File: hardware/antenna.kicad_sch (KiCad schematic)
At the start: 8 parts

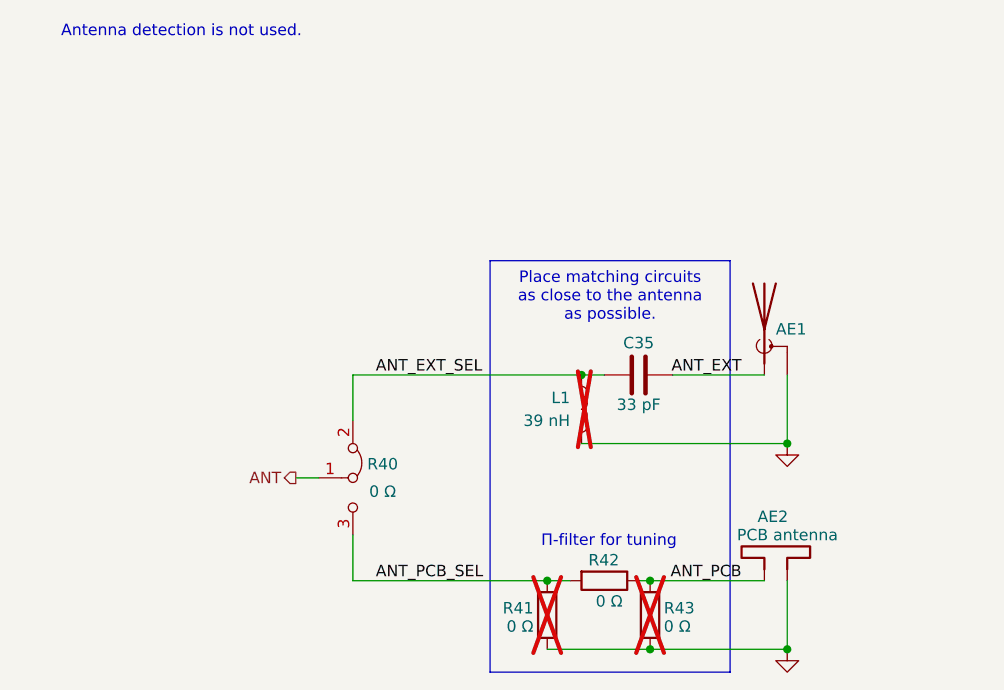
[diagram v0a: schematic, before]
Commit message: HW: Update components to be hand solderable
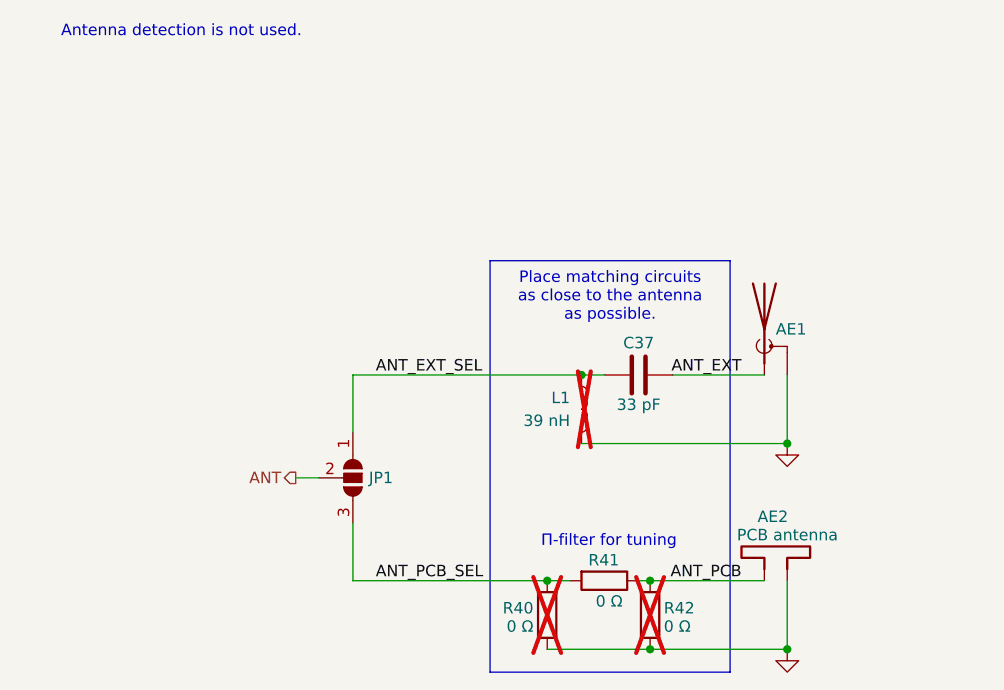
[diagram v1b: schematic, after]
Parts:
- removed R40: 0 Ω, perfect_footprints:0hm_choice, symbol perfect_footprints:0hm_choice
- added JP1: SolderJumper_3_Open, Jumper:SolderJumper-3_P2.0mm_Open_TrianglePad1.0x1.5mm, symbol Jumper:SolderJumper_3_Open
- C37: renamed from C35; footprint perfect_footprints:0402_1005_perfect -> Capacitor_SMD:C_0402_1005Metric_Pad0.74x0.62mm_HandSolder
- L1: footprint Inductor_SMD:L_0603_1608Metric -> Inductor_SMD:L_0603_1608Metric_Pad1.05x0.95mm_HandSolder
- R40: renamed from R41; footprint perfect_footprints:0402_1005_perfect -> Resistor_SMD:R_0402_1005Metric_Pad0.72x0.64mm_HandSolder
- R41: renamed from R42; footprint perfect_footprints:0402_1005_perfect -> Resistor_SMD:R_0402_1005Metric_Pad0.72x0.64mm_HandSolder
- R42: renamed from R43; footprint perfect_footprints:0402_1005_perfect -> Resistor_SMD:R_0402_1005Metric_Pad0.72x0.64mm_HandSolder
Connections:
- net ANT: now also JP1.2 (C)
- net ANT_EXT_SEL: now also JP1.1 (A)
- net ANT_PCB_SEL: now also JP1.3 (B)
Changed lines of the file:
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@@
 	(wire
 		(pts
-			(xy 101.6 106.68) (xy 101.6 111.76)
+			(xy 101.6 105.41) (xy 101.6 111.76)
 		)
 		(stroke
@@
 	(wire
 		(pts
-			(xy 101.6 88.9) (xy 101.6 93.98)
+			(xy 147.32 111.76) (xy 134.62 111.76)
 		)
 		(stroke
@@
 	(wire
 		(pts
-			(xy 147.32 111.76) (xy 134.62 111.76)
+			(xy 125.73 111.76) (xy 123.19 111.76)
 		)
 		(stroke
@@
 	(wire
 		(pts
-			(xy 125.73 111.76) (xy 123.19 111.76)
+			(xy 101.6 88.9) (xy 127 88.9)
 		)
 		(stroke
@@
 	(wire
 		(pts
-			(xy 101.6 88.9) (xy 127 88.9)
+			(xy 147.32 88.9) (xy 137.16 88.9)
 		)
 		(stroke
@@
 	(wire
 		(pts
-			(xy 147.32 88.9) (xy 137.16 88.9)
+			(xy 149.86 119.38) (xy 134.62 119.38)
 		)
 		(stroke
@@
 	(wire
 		(pts
-			(xy 149.86 119.38) (xy 134.62 119.38)
+			(xy 134.62 111.76) (xy 133.35 111.76)
 		)
 		(stroke
@@
 	(wire
 		(pts
-			(xy 134.62 111.76) (xy 133.35 111.76)
+			(xy 101.6 88.9) (xy 101.6 95.25)
 		)
 		(stroke
@@
 		(on_board yes)
 		(dnp no)
-		(property "Reference" "C35"
+		(property "Reference" "C37"
 			(at 133.35 85.344 90)
 			(effects
@@
 			)
 		)
-		(property "Footprint" "perfect_footprints:0402_1005_perfect"
+		(property "Footprint" "Capacitor_SMD:C_0402_1005Metric_Pad0.74x0.62mm_HandSolder"
 			(at 129.54 87.9348 0)
 			(effects
@@
 			(project "iida_devkit"
 				(path "/b12a6e25-97fb-4aba-bc96-af8db389bb9a/6e456e95-dbda-43fc-b148-815c3be21ba0"
-					(reference "C35")
+					(reference "C37")
 					(unit 1)
 				)
@@
 		(on_board yes)
 		(dnp no)
-		(property "Reference" "R42"
+		(property "Reference" "R41"
 			(at 127.762 109.474 90)
 			(effects
@@
 			)
 		)
-		(property "Footprint" "perfect_footprints:0402_1005_perfect"
+		(property "Footprint" "Resistor_SMD:R_0402_1005Metric_Pad0.72x0.64mm_HandSolder"
 			(at 129.54 109.982 90)
 			(effects
@@
 			(project "iida_devkit"
 				(path "/b12a6e25-97fb-4aba-bc96-af8db389bb9a/6e456e95-dbda-43fc-b148-815c3be21ba0"
-					(reference "R42")
+					(reference "R41")
 					(unit 1)
 				)
@@
 			)
 		)
-		(property "Footprint" "Inductor_SMD:L_0603_1608Metric"
+		(property "Footprint" "Inductor_SMD:L_0603_1608Metric_Pad1.05x0.95mm_HandSolder"
 			(at 127 92.71 0)
 			(effects
@@
 		(dnp no)
 		(fields_autoplaced yes)
-		(property "Reference" "#PWR054"
+		(property "Reference" "#PWR060"
 			(at 149.86 125.73 0)
 			(effects
@@
 			(project "iida_devkit"
 				(path "/b12a6e25-97fb-4aba-bc96-af8db389bb9a/6e456e95-dbda-43fc-b148-815c3be21ba0"
-					(reference "#PWR054")
+					(reference "#PWR060")
 					(unit 1)
 				)
@@
 		(on_board yes)
 		(dnp yes)
-		(property "Reference" "R41"
+		(property "Reference" "R40"
 			(at 121.666 114.808 0)
 			(effects
@@
 			)
 		)
-		(property "Footprint" "perfect_footprints:0402_1005_perfect"
+		(property "Footprint" "Resistor_SMD:R_0402_1005Metric_Pad0.72x0.64mm_HandSolder"
 			(at 121.412 115.57 90)
 			(effects
@@
 			(project "iida_devkit"
 				(path "/b12a6e25-97fb-4aba-bc96-af8db389bb9a/6e456e95-dbda-43fc-b148-815c3be21ba0"
-					(reference "R41")
+					(reference "R40")
 					(unit 1)
 				)
@@
 		(on_board yes)
 		(dnp yes)
-		(property "Reference" "R43"
+		(property "Reference" "R42"
 			(at 136.144 114.808 0)
 			(effects
@@
 			)
 		)
-		(property "Footprint" "perfect_footprints:0402_1005_perfect"
+		(property "Footprint" "Resistor_SMD:R_0402_1005Metric_Pad0.72x0.64mm_HandSolder"
 			(at 136.398 115.57 90)
 			(effects
@@
 			(project "iida_devkit"
 				(path "/b12a6e25-97fb-4aba-bc96-af8db389bb9a/6e456e95-dbda-43fc-b148-815c3be21ba0"
-					(reference "R43")
+					(reference "R42")
 					(unit 1)
 				)
@@
 	)
 	(symbol
-		(lib_id "perfect_footprints:0hm_choice")
+		(lib_id "Jumper:SolderJumper_3_Open")
 		(at 101.6 100.33 270)
 		(unit 1)
-		(exclude_from_sim no)
-		(in_bom yes)
+		(exclude_from_sim yes)
+		(in_bom no)
 		(on_board yes)
 		(dnp no)
-		(property "Reference" "R40"
-			(at 104.902 98.806 90)
+		(property "Reference" "JP1"
+			(at 103.378 100.33 90)
 			(effects
 				(font
 					(size 1.27 1.27)
 				)
+				(justify left)
 			)
 		)
-		(property "Value" "0 Ω"
-			(at 104.902 101.854 90)
+		(property "Value" "SolderJumper_3_Open"
+			(at 104.14 101.5999 90)
 			(effects
 				(font
 					(size 1.27 1.27)
 				)
+				(justify left)
+				(hide yes)
 			)
 		)
-		(property "Footprint" "perfect_footprints:0hm_choice"
-			(at 93.472 100.33 0)
+		(property "Footprint" "Jumper:SolderJumper-3_P2.0mm_Open_TrianglePad1.0x1.5mm"
+			(at 101.6 100.33 0)
 			(effects
 				(font
@@
 			)
 		)
-		(property "Datasheet" ""
-			(at 105.41 95.25 0)
+		(property "Datasheet" "~"
+			(at 101.6 100.33 0)
 			(effects
 				(font
@@
 			)
 		)
-		(property "Description" ""
-			(at 105.41 95.25 0)
+		(property "Description" "Solder Jumper, 3-pole, open"
+			(at 101.6 100.33 0)
 			(effects
 				(font
@@
 			)
 		)
-		(property "Digi-Key Part Number" "311-0.0JRCT-ND"
+		(property "Digi-Key Part Number" "-"
 			(at 101.6 100.33 0)
 			(effects
@@
 			)
 		)
-		(property "Manufacturer" "YAGEO"
+		(property "Manufacturer" "-"
 			(at 101.6 100.33 0)
 			(effects
@@
 			)
 		)
-		(property "Manufacturer Part Number" "RC0402JR-070RL"
+		(property "Manufacturer Part Number" "-"
 			(at 101.6 100.33 0)
 			(effects
@@
 		(pin "2"
 		)
-		(pin "3"
-		)
 		(pin "1"
 		)
+		(pin "3"
+		)
 		(instances
 			(project ""
 				(path "/b12a6e25-97fb-4aba-bc96-af8db389bb9a/6e456e95-dbda-43fc-b148-815c3be21ba0"
-					(reference "R40")
+					(reference "JP1")
 					(unit 1)
 				)
@@
 		(dnp no)
 		(fields_autoplaced yes)
-		(property "Reference" "#PWR053"
+		(property "Reference" "#PWR059"
 			(at 149.86 102.87 0)
 			(effects
@@
 			(project "iida_devkit"
 				(path "/b12a6e25-97fb-4aba-bc96-af8db389bb9a/6e456e95-dbda-43fc-b148-815c3be21ba0"
-					(reference "#PWR053")
+					(reference "#PWR059")
 					(unit 1)
 				)

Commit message: HW: Update components, change footprints to handsolder versions, finish power
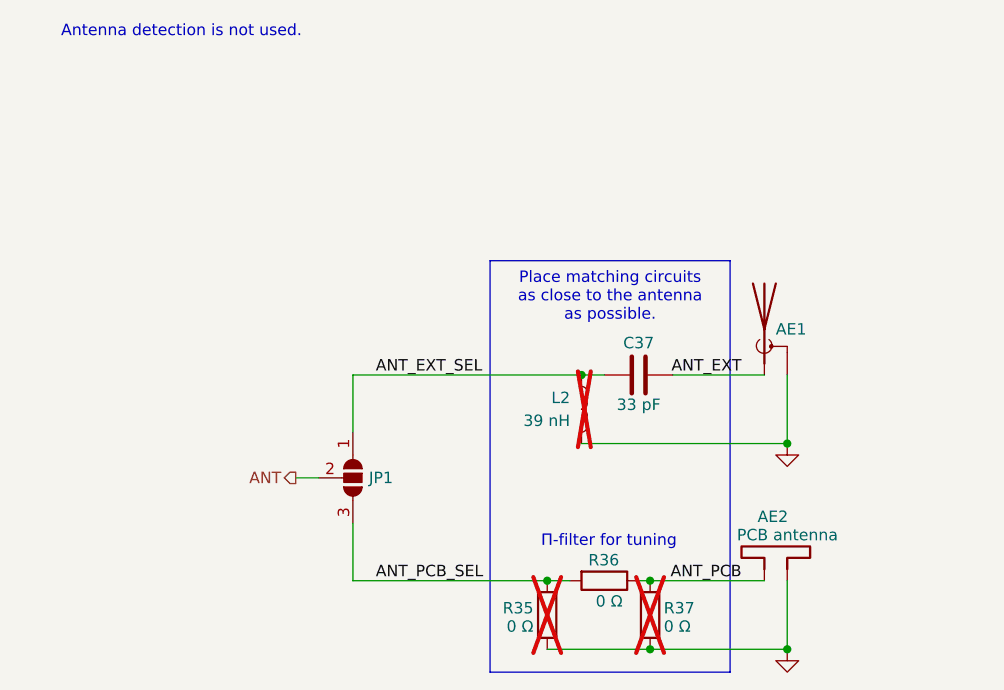
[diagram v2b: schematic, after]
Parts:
- R35: renamed from R40; Digi-Key Part Number 311-0.0JRCT-ND -> 732-560112110001CT-ND; Manufacturer YAGEO -> Würth Elektronik; Manufacturer Part Number RC0402JR-070RL -> 560112110001
- R36: renamed from R41; Digi-Key Part Number 311-0.0JRCT-ND -> 732-560112110001CT-ND; Manufacturer YAGEO -> Würth Elektronik; Manufacturer Part Number RC0402JR-070RL -> 560112110001
- R37: renamed from R42; Digi-Key Part Number 311-0.0JRCT-ND -> 732-560112110001CT-ND; Manufacturer YAGEO -> Würth Elektronik; Manufacturer Part Number RC0402JR-070RL -> 560112110001
- renumbered L1 to L2
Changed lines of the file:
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@@
 		(on_board yes)
 		(dnp no)
-		(property "Reference" "R41"
+		(property "Reference" "R36"
 			(at 127.762 109.474 90)
 			(effects
@@
 			)
 		)
-		(property "Manufacturer" "YAGEO"
+		(property "Manufacturer" "Würth Elektronik"
 			(at 129.54 111.76 0)
 			(effects
@@
 			)
 		)
-		(property "Manufacturer Part Number" "RC0402JR-070RL"
+		(property "Manufacturer Part Number" "560112110001"
 			(at 129.54 111.76 0)
 			(effects
@@
 			)
 		)
-		(property "Digi-Key Part Number" "311-0.0JRCT-ND"
+		(property "Digi-Key Part Number" "732-560112110001CT-ND"
 			(at 129.54 111.76 0)
 			(effects
@@
 			(project "iida_devkit"
 				(path "/b12a6e25-97fb-4aba-bc96-af8db389bb9a/6e456e95-dbda-43fc-b148-815c3be21ba0"
-					(reference "R41")
+					(reference "R36")
 					(unit 1)
 				)
@@
 		(on_board yes)
 		(dnp yes)
-		(property "Reference" "L1"
+		(property "Reference" "L2"
 			(at 125.73 91.4399 0)
 			(effects
@@
 			(project "iida_devkit"
 				(path "/b12a6e25-97fb-4aba-bc96-af8db389bb9a/6e456e95-dbda-43fc-b148-815c3be21ba0"
-					(reference "L1")
+					(reference "L2")
 					(unit 1)
 				)
@@
 		(dnp no)
 		(fields_autoplaced yes)
-		(property "Reference" "#PWR060"
+		(property "Reference" "#PWR058"
 			(at 149.86 125.73 0)
 			(effects
@@
 			(project "iida_devkit"
 				(path "/b12a6e25-97fb-4aba-bc96-af8db389bb9a/6e456e95-dbda-43fc-b148-815c3be21ba0"
-					(reference "#PWR060")
+					(reference "#PWR058")
 					(unit 1)
 				)
@@
 		(on_board yes)
 		(dnp yes)
-		(property "Reference" "R40"
+		(property "Reference" "R35"
 			(at 121.666 114.808 0)
 			(effects
@@
 			)
 		)
-		(property "Manufacturer" "YAGEO"
+		(property "Manufacturer" "Würth Elektronik"
 			(at 123.19 115.57 0)
 			(effects
@@
 			)
 		)
-		(property "Manufacturer Part Number" "RC0402JR-070RL"
+		(property "Manufacturer Part Number" "560112110001"
 			(at 123.19 115.57 0)
 			(effects
@@
 			)
 		)
-		(property "Digi-Key Part Number" "311-0.0JRCT-ND"
+		(property "Digi-Key Part Number" "732-560112110001CT-ND"
 			(at 123.19 115.57 0)
 			(effects
@@
 			(project "iida_devkit"
 				(path "/b12a6e25-97fb-4aba-bc96-af8db389bb9a/6e456e95-dbda-43fc-b148-815c3be21ba0"
-					(reference "R40")
+					(reference "R35")
 					(unit 1)
 				)
@@
 		(on_board yes)
 		(dnp yes)
-		(property "Reference" "R42"
+		(property "Reference" "R37"
 			(at 136.144 114.808 0)
 			(effects
@@
 			)
 		)
-		(property "Manufacturer" "YAGEO"
+		(property "Manufacturer" "Würth Elektronik"
 			(at 134.62 115.57 0)
 			(effects
@@
 			)
 		)
-		(property "Manufacturer Part Number" "RC0402JR-070RL"
+		(property "Manufacturer Part Number" "560112110001"
 			(at 134.62 115.57 0)
 			(effects
@@
 			)
 		)
-		(property "Digi-Key Part Number" "311-0.0JRCT-ND"
+		(property "Digi-Key Part Number" "732-560112110001CT-ND"
 			(at 134.62 115.57 0)
 			(effects
@@
 			(project "iida_devkit"
 				(path "/b12a6e25-97fb-4aba-bc96-af8db389bb9a/6e456e95-dbda-43fc-b148-815c3be21ba0"
-					(reference "R42")
+					(reference "R37")
 					(unit 1)
 				)
@@
 		(dnp no)
 		(fields_autoplaced yes)
-		(property "Reference" "#PWR059"
+		(property "Reference" "#PWR057"
 			(at 149.86 102.87 0)
 			(effects
@@
 			(project "iida_devkit"
 				(path "/b12a6e25-97fb-4aba-bc96-af8db389bb9a/6e456e95-dbda-43fc-b148-815c3be21ba0"
-					(reference "#PWR059")
-					(unit 1)
-				)
+					(reference "#PWR057")
+					(unit 1)
+				)

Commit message: HW: Add battery protection
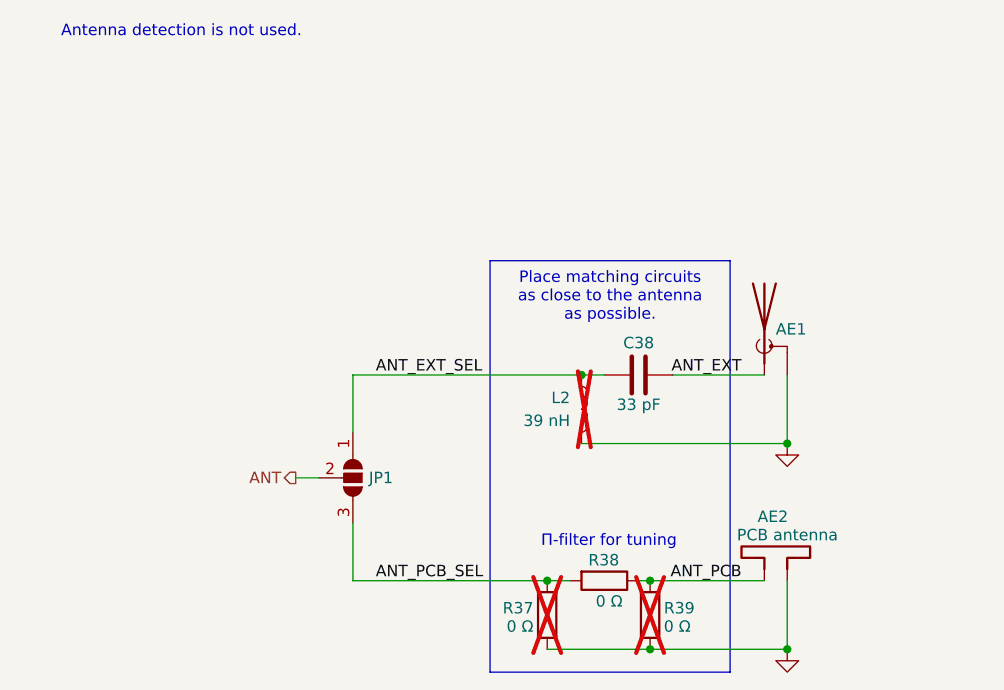
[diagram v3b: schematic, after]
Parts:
- renumbered C37 to C38, R35 to R37, R36 to R38, R37 to R39
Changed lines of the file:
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@@
 		(on_board yes)
 		(dnp no)
-		(property "Reference" "C37"
+		(property "Reference" "C38"
 			(at 133.35 85.344 90)
 			(effects
@@
 			(project "iida_devkit"
 				(path "/b12a6e25-97fb-4aba-bc96-af8db389bb9a/6e456e95-dbda-43fc-b148-815c3be21ba0"
-					(reference "C37")
+					(reference "C38")
 					(unit 1)
 				)
@@
 		(on_board yes)
 		(dnp no)
-		(property "Reference" "R36"
+		(property "Reference" "R38"
 			(at 127.762 109.474 90)
 			(effects
@@
 			(project "iida_devkit"
 				(path "/b12a6e25-97fb-4aba-bc96-af8db389bb9a/6e456e95-dbda-43fc-b148-815c3be21ba0"
-					(reference "R36")
+					(reference "R38")
 					(unit 1)
 				)
@@
 		(dnp no)
 		(fields_autoplaced yes)
-		(property "Reference" "#PWR058"
+		(property "Reference" "#PWR060"
 			(at 149.86 125.73 0)
 			(effects
@@
 			(project "iida_devkit"
 				(path "/b12a6e25-97fb-4aba-bc96-af8db389bb9a/6e456e95-dbda-43fc-b148-815c3be21ba0"
-					(reference "#PWR058")
+					(reference "#PWR060")
 					(unit 1)
 				)
@@
 		(on_board yes)
 		(dnp yes)
-		(property "Reference" "R35"
+		(property "Reference" "R37"
 			(at 121.666 114.808 0)
 			(effects
@@
 			(project "iida_devkit"
 				(path "/b12a6e25-97fb-4aba-bc96-af8db389bb9a/6e456e95-dbda-43fc-b148-815c3be21ba0"
-					(reference "R35")
+					(reference "R37")
 					(unit 1)
 				)
@@
 		(on_board yes)
 		(dnp yes)
-		(property "Reference" "R37"
+		(property "Reference" "R39"
 			(at 136.144 114.808 0)
 			(effects
@@
 			(project "iida_devkit"
 				(path "/b12a6e25-97fb-4aba-bc96-af8db389bb9a/6e456e95-dbda-43fc-b148-815c3be21ba0"
-					(reference "R37")
+					(reference "R39")
 					(unit 1)
 				)
@@
 		(dnp no)
 		(fields_autoplaced yes)
-		(property "Reference" "#PWR057"
+		(property "Reference" "#PWR059"
 			(at 149.86 102.87 0)
 			(effects
@@
 			(project "iida_devkit"
 				(path "/b12a6e25-97fb-4aba-bc96-af8db389bb9a/6e456e95-dbda-43fc-b148-815c3be21ba0"
-					(reference "#PWR057")
-					(unit 1)
-				)
+					(reference "#PWR059")
+					(unit 1)
+				)

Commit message: HW: Replace 0402 with 0603 or bigger
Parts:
- C38: footprint Capacitor_SMD:C_0402_1005Metric_Pad0.74x0.62mm_HandSolder -> Capacitor_SMD:C_0603_1608Metric_Pad1.08x0.95mm_HandSolder; Digi-Key Part Number 732-7472-1-ND -> 732-7749-1-ND; Manufacturer Part Number 885012005058 -> 885012006005
- R37, R38, R39: footprint Resistor_SMD:R_0402_1005Metric_Pad0.72x0.64mm_HandSolder -> Resistor_SMD:R_0805_2012Metric_Pad1.20x1.40mm_HandSolder; Digi-Key Part Number 732-560112110001CT-ND -> 732-560112120002CT-ND; Manufacturer Part Number 560112110001 -> 560112120002
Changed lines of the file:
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@@
 			)
 		)
-		(property "Footprint" "Capacitor_SMD:C_0402_1005Metric_Pad0.74x0.62mm_HandSolder"
+		(property "Footprint" "Capacitor_SMD:C_0603_1608Metric_Pad1.08x0.95mm_HandSolder"
 			(at 129.54 87.9348 0)
 			(effects
@@
 			)
 		)
-		(property "Digi-Key Part Number" "732-7472-1-ND"
+		(property "Digi-Key Part Number" "732-7749-1-ND"
 			(at 133.35 88.9 0)
 			(effects
@@
 			)
 		)
-		(property "Manufacturer Part Number" "885012005058"
+		(property "Manufacturer Part Number" "885012006005"
 			(at 133.35 88.9 0)
 			(effects
@@
 			)
 		)
-		(property "Footprint" "Resistor_SMD:R_0402_1005Metric_Pad0.72x0.64mm_HandSolder"
+		(property "Footprint" "Resistor_SMD:R_0805_2012Metric_Pad1.20x1.40mm_HandSolder"
 			(at 129.54 109.982 90)
 			(effects
@@
 			)
 		)
-		(property "Manufacturer Part Number" "560112110001"
+		(property "Manufacturer Part Number" "560112120002"
 			(at 129.54 111.76 0)
 			(effects
@@
 			)
 		)
-		(property "Digi-Key Part Number" "732-560112110001CT-ND"
+		(property "Digi-Key Part Number" "732-560112120002CT-ND"
 			(at 129.54 111.76 0)
 			(effects
@@
 			)
 		)
-		(property "Footprint" "Resistor_SMD:R_0402_1005Metric_Pad0.72x0.64mm_HandSolder"
+		(property "Footprint" "Resistor_SMD:R_0805_2012Metric_Pad1.20x1.40mm_HandSolder"
 			(at 121.412 115.57 90)
 			(effects
@@
 			)
 		)
-		(property "Manufacturer Part Number" "560112110001"
+		(property "Manufacturer Part Number" "560112120002"
 			(at 123.19 115.57 0)
 			(effects
@@
 			)
 		)
-		(property "Digi-Key Part Number" "732-560112110001CT-ND"
+		(property "Digi-Key Part Number" "732-560112120002CT-ND"
 			(at 123.19 115.57 0)
 			(effects
@@
 			)
 		)
-		(property "Footprint" "Resistor_SMD:R_0402_1005Metric_Pad0.72x0.64mm_HandSolder"
+		(property "Footprint" "Resistor_SMD:R_0805_2012Metric_Pad1.20x1.40mm_HandSolder"
 			(at 136.398 115.57 90)
 			(effects
@@
 			)
 		)
-		(property "Manufacturer Part Number" "560112110001"
+		(property "Manufacturer Part Number" "560112120002"
 			(at 134.62 115.57 0)
 			(effects
@@
 			)
 		)
-		(property "Digi-Key Part Number" "732-560112110001CT-ND"
+		(property "Digi-Key Part Number" "732-560112120002CT-ND"
 			(at 134.62 115.57 0)
 			(effects
